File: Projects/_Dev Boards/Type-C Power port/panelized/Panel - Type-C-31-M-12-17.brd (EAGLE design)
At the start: 100 x 100 mm, 40 parts, among them J1 USB-TYPE-C-31-M-17, J10 USB-TYPE-C-31-M-12, J11 USB-TYPE-C-31-M-12, J12 USB-TYPE-C-31-M-12, J13 USB-TYPE-C-31-M-12, J14 USB-TYPE-C-31-M-12, J15 USB-TYPE-C-31-M-12, J16 USB-TYPE-C-31-M-17, J17 USB-TYPE-C-31-M-17, J18 USB-TYPE-C-31-M-17, J19 USB-TYPE-C-31-M-17, J2 USB-TYPE-C-31-M-12, J20 USB-TYPE-C-31-M-17, J3 USB-TYPE-C-31-M-17, J4 USB-TYPE-C-31-M-17, J5 USB-TYPE-C-31-M-17, J6 USB-TYPE-C-31-M-17, J7 USB-TYPE-C-31-M-12, J8 USB-TYPE-C-31-M-12, J9 USB-TYPE-C-31-M-12

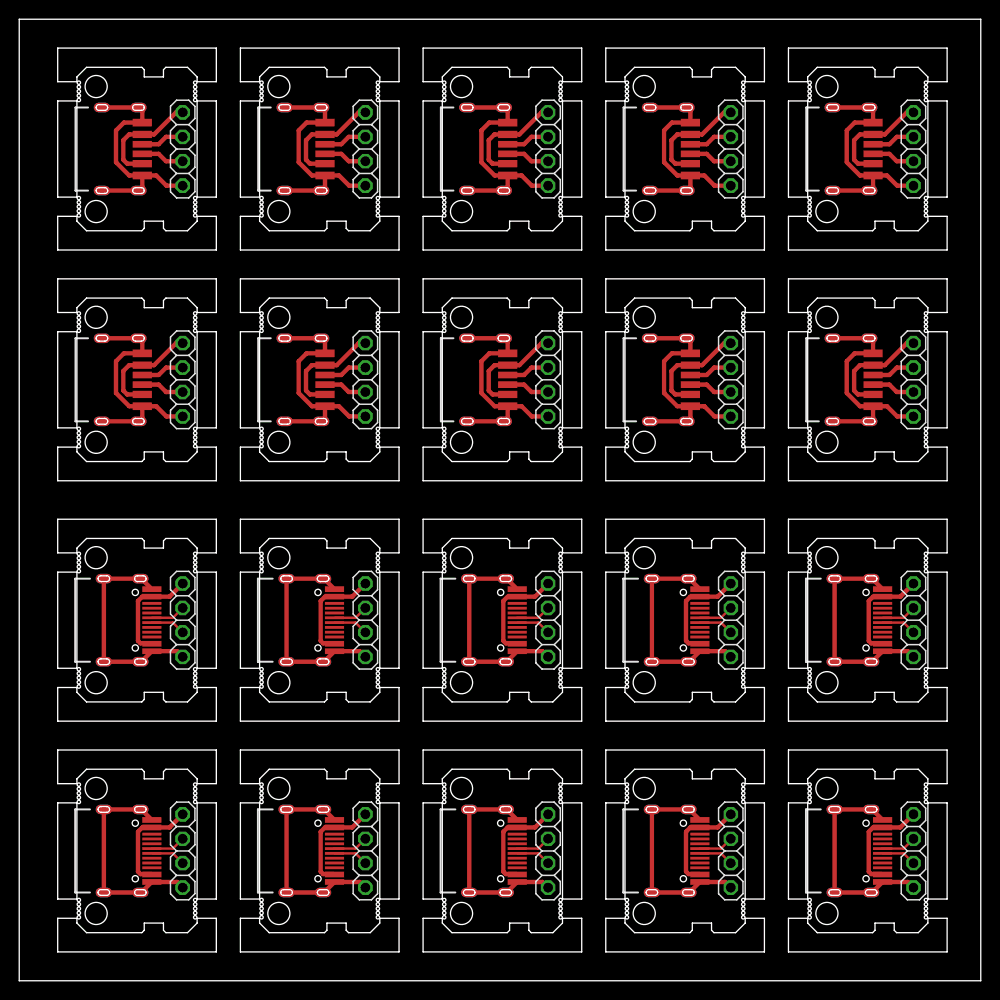
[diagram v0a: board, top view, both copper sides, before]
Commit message: updated Type-C power board
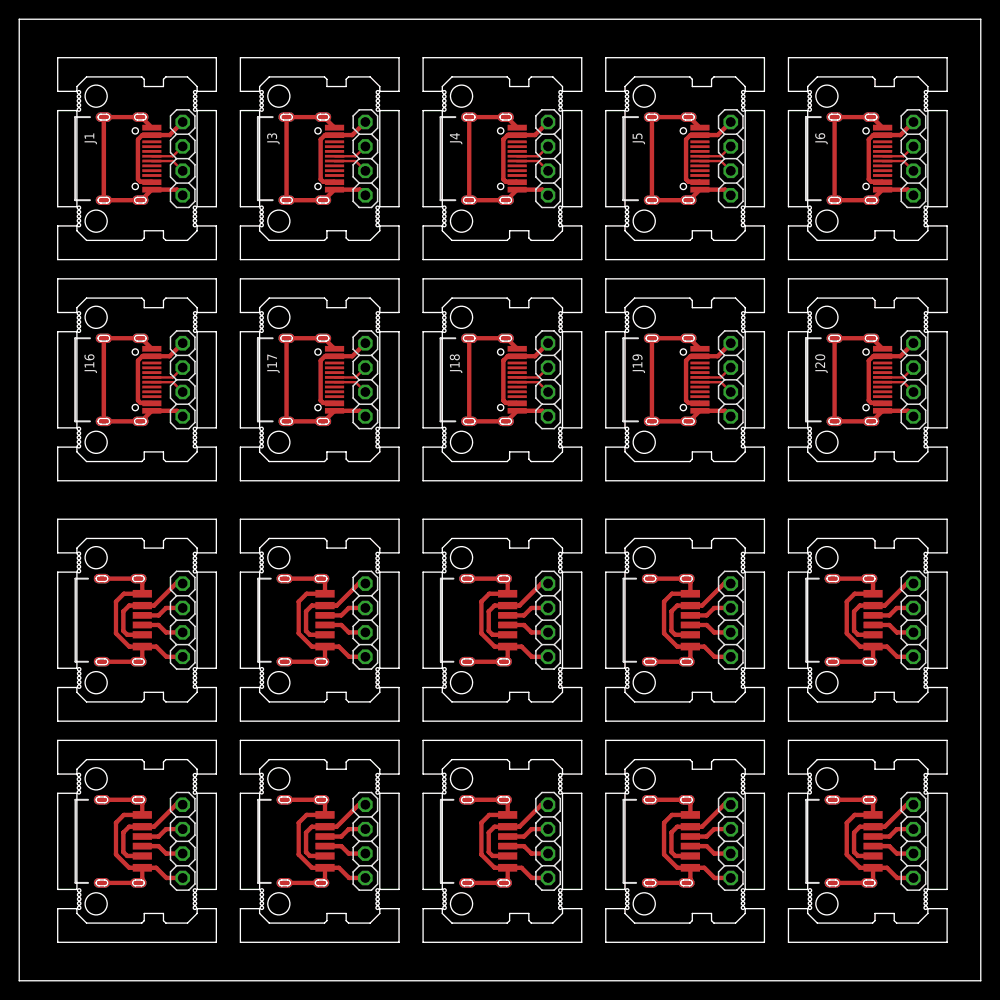
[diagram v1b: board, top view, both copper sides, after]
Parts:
- J1, J16, J17, J18, J19, J20, J3, J4, J5, J6: value USB-TYPE-C-31-M-17 -> USB-TYPE-C-31-M-12; device angrypig7-Connectors:USB-TYPE-C-31-M-17 -> angrypig7-Connectors:USB-TYPE-C-31-M-12
- J10, J11, J12, J13, J14, J15, J2, J7, J8, J9: value USB-TYPE-C-31-M-12 -> USB-TYPE-C-31-M-17; device angrypig7-Connectors:USB-TYPE-C-31-M-12 -> angrypig7-Connectors:USB-TYPE-C-31-M-17
- moved JP1 72.0 mm to (17.0, 14.5)
- moved JP2 72.0 mm to (17.0, 85.5)
- moved J3 1.02 mm to (31.6, 85.5)
- moved J4 1.02 mm to (50.6, 85.5)
- moved J7 1.02 mm to (31.4, 14.5)
- moved J8 1.02 mm to (50.4, 14.5)
- moved J1 1.02 mm to (12.6, 85.5)
- moved J2 1.02 mm to (12.4, 14.5)
- moved J10 1.02 mm to (88.4, 14.5)
- moved J5 1.02 mm to (69.6, 85.5)
- moved J6 1.02 mm to (88.6, 85.5)
- moved J9 1.02 mm to (69.4, 14.5)
- moved JP10 1.00 mm to (93.0, 14.5)
- moved JP3 1.00 mm to (36.0, 85.5)
- moved JP4 1.00 mm to (55.0, 85.5)
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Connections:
- new net N$61: J16.VBUS1, J16.VBUS2, JP16.1
- new net N$62: J16.A6, JP16.2
- new net N$63: J16.A7, JP16.3
- new net N$64: J16.GND1, J16.GND2, J16.SHLD-B1, J16.SHLD-B2, J16.SHLD-B3, J16.SHLD-B4, J16.SHLD-T1, J16.SHLD-T2, J16.SHLD-T3, J16.SHLD-T4, JP16.4
- new net N$65: J17.VBUS1, J17.VBUS2, JP17.1
- new net N$66: J17.A6, JP17.2
- new net N$67: J17.A7, JP17.3
- new net N$68: J17.GND1, J17.GND2, J17.SHLD-B1, J17.SHLD-B2, J17.SHLD-B3, J17.SHLD-B4, J17.SHLD-T1, J17.SHLD-T2, J17.SHLD-T3, J17.SHLD-T4, JP17.4
- new net N$69: J18.VBUS1, J18.VBUS2, JP18.1
- new net N$70: J18.A6, JP18.2
- new net N$71: J18.A7, JP18.3
- new net N$72: J18.GND1, J18.GND2, J18.SHLD-B1, J18.SHLD-B2, J18.SHLD-B3, J18.SHLD-B4, J18.SHLD-T1, J18.SHLD-T2, J18.SHLD-T3, J18.SHLD-T4, JP18.4
- new net N$73: J19.VBUS1, J19.VBUS2, JP19.1
- new net N$74: J19.A6, JP19.2
- new net N$75: J19.A7, JP19.3
- new net N$76: J19.GND1, J19.GND2, J19.SHLD-B1, J19.SHLD-B2, J19.SHLD-B3, J19.SHLD-B4, J19.SHLD-T1, J19.SHLD-T2, J19.SHLD-T3, J19.SHLD-T4, JP19.4
- new net N$77: J20.VBUS1, J20.VBUS2, JP20.1
- new net N$78: J20.A6, JP20.2
- new net N$79: J20.A7, JP20.3
- new net N$80: J20.GND1, J20.GND2, J20.SHLD-B1, J20.SHLD-B2, J20.SHLD-B3, J20.SHLD-B4, J20.SHLD-T1, J20.SHLD-T2, J20.SHLD-T3, J20.SHLD-T4, JP20.4
- net N$1: now also J1.VBUS1, J1.VBUS2, JP2.1; no longer J1.GND, J1.GND_2, J1.SHLD-B1, J1.SHLD-B2, J1.SHLD-B3, J1.SHLD-B4, J1.SHLD-T1, J1.SHLD-T2, J1.SHLD-T3, J1.SHLD-T4, JP1.4
- net N$10: now also J3.A6, JP3.2; no longer J3.VBUS, J3.VBUS_2, JP3.1
- net N$11: now also J3.A7, JP3.3; no longer J3.CC1, JP3.2
- net N$12: now also J3.GND1, J3.GND2, J3.SHLD-B1, J3.SHLD-B2, J3.SHLD-B3, J3.SHLD-B4, J3.SHLD-T1, J3.SHLD-T2, J3.SHLD-T3, J3.SHLD-T4, JP3.4; no longer J3.CC2, JP3.3
- net N$13: now also J4.VBUS1, J4.VBUS2, JP4.1; no longer J4.GND, J4.GND_2, J4.SHLD-B1, J4.SHLD-B2, J4.SHLD-B3, J4.SHLD-B4, J4.SHLD-T1, J4.SHLD-T2, J4.SHLD-T3, J4.SHLD-T4, JP4.4
- net N$14: now also J4.A6, JP4.2; no longer J4.VBUS, J4.VBUS_2, JP4.1
- net N$15: now also J4.A7, JP4.3; no longer J4.CC1, JP4.2
- net N$16: now also J4.GND1, J4.GND2, J4.SHLD-B1, J4.SHLD-B2, J4.SHLD-B3, J4.SHLD-B4, J4.SHLD-T1, J4.SHLD-T2, J4.SHLD-T3, J4.SHLD-T4, JP4.4; no longer J4.CC2, JP4.3
- net N$17: now also J5.VBUS1, J5.VBUS2, JP5.1; no longer J5.GND, J5.GND_2, J5.SHLD-B1, J5.SHLD-B2, J5.SHLD-B3, J5.SHLD-B4, J5.SHLD-T1, J5.SHLD-T2, J5.SHLD-T3, J5.SHLD-T4, JP5.4
- net N$18: now also J5.A6, JP5.2; no longer J5.VBUS, J5.VBUS_2, JP5.1
- net N$19: now also J5.A7, JP5.3; no longer J5.CC1, JP5.2
- net N$2: now also J1.A6, JP2.2; no longer J1.VBUS, J1.VBUS_2, JP1.1
- net N$20: now also J5.GND1, J5.GND2, J5.SHLD-B1, J5.SHLD-B2, J5.SHLD-B3, J5.SHLD-B4, J5.SHLD-T1, J5.SHLD-T2, J5.SHLD-T3, J5.SHLD-T4, JP5.4; no longer J5.CC2, JP5.3
- net N$21: now also J6.VBUS1, J6.VBUS2, JP6.1; no longer J6.GND, J6.GND_2, J6.SHLD-B1, J6.SHLD-B2, J6.SHLD-B3, J6.SHLD-B4, J6.SHLD-T1, J6.SHLD-T2, J6.SHLD-T3, J6.SHLD-T4, JP6.4
- net N$22: now also J6.A6, JP6.2; no longer J6.VBUS, J6.VBUS_2, JP6.1
- net N$23: now also J6.A7, JP6.3; no longer J6.CC1, JP6.2
- net N$24: now also J6.GND1, J6.GND2, J6.SHLD-B1, J6.SHLD-B2, J6.SHLD-B3, J6.SHLD-B4, J6.SHLD-T1, J6.SHLD-T2, J6.SHLD-T3, J6.SHLD-T4, JP6.4; no longer J6.CC2, JP6.3
- net N$25: now also J7.GND, J7.GND_2, J7.SHLD-B1, J7.SHLD-B2, J7.SHLD-B3, J7.SHLD-B4, J7.SHLD-T1, J7.SHLD-T2, J7.SHLD-T3, J7.SHLD-T4, JP7.4; no longer J7.VBUS1, J7.VBUS2, JP7.1
- net N$26: now also J7.VBUS, J7.VBUS_2, JP7.1; no longer J7.A6, JP7.2
- net N$27: now also J7.CC1, JP7.2; no longer J7.A7, JP7.3
- net N$28: now also J7.CC2, JP7.3; no longer J7.GND1, J7.GND2, J7.SHLD-B1, J7.SHLD-B2, J7.SHLD-B3, J7.SHLD-B4, J7.SHLD-T1, J7.SHLD-T2, J7.SHLD-T3, J7.SHLD-T4, JP7.4
- net N$29: now also J8.GND, J8.GND_2, J8.SHLD-B1, J8.SHLD-B2, J8.SHLD-B3, J8.SHLD-B4, J8.SHLD-T1, J8.SHLD-T2, J8.SHLD-T3, J8.SHLD-T4, JP8.4; no longer J8.VBUS1, J8.VBUS2, JP8.1
- net N$3: now also J1.A7, JP2.3; no longer J1.CC1, JP1.2
- net N$30: now also J8.VBUS, J8.VBUS_2, JP8.1; no longer J8.A6, JP8.2
- net N$31: now also J8.CC1, JP8.2; no longer J8.A7, JP8.3
- net N$32: now also J8.CC2, JP8.3; no longer J8.GND1, J8.GND2, J8.SHLD-B1, J8.SHLD-B2, J8.SHLD-B3, J8.SHLD-B4, J8.SHLD-T1, J8.SHLD-T2, J8.SHLD-T3, J8.SHLD-T4, JP8.4
- net N$33: now also J9.GND, J9.GND_2, J9.SHLD-B1, J9.SHLD-B2, J9.SHLD-B3, J9.SHLD-B4, J9.SHLD-T1, J9.SHLD-T2, J9.SHLD-T3, J9.SHLD-T4, JP9.4; no longer J9.VBUS1, J9.VBUS2, JP9.1
- net N$34: now also J9.VBUS, J9.VBUS_2, JP9.1; no longer J9.A6, JP9.2
- net N$35: now also J9.CC1, JP9.2; no longer J9.A7, JP9.3
- net N$36: now also J9.CC2, JP9.3; no longer J9.GND1, J9.GND2, J9.SHLD-B1, J9.SHLD-B2, J9.SHLD-B3, J9.SHLD-B4, J9.SHLD-T1, J9.SHLD-T2, J9.SHLD-T3, J9.SHLD-T4, JP9.4
- net N$37: now also J10.GND, J10.GND_2, J10.SHLD-B1, J10.SHLD-B2, J10.SHLD-B3, J10.SHLD-B4, J10.SHLD-T1, J10.SHLD-T2, J10.SHLD-T3, J10.SHLD-T4, JP10.4; no longer J10.VBUS1, J10.VBUS2, JP10.1
- net N$38: now also J10.VBUS, J10.VBUS_2, JP10.1; no longer J10.A6, JP10.2
- net N$39: now also J10.CC1, JP10.2; no longer J10.A7, JP10.3
- net N$4: now also J1.GND1, J1.GND2, J1.SHLD-B1, J1.SHLD-B2, J1.SHLD-B3, J1.SHLD-B4, J1.SHLD-T1, J1.SHLD-T2, J1.SHLD-T3, J1.SHLD-T4, JP2.4; no longer J1.CC2, JP1.3
- net N$40: now also J10.CC2, JP10.3; no longer J10.GND1, J10.GND2, J10.SHLD-B1, J10.SHLD-B2, J10.SHLD-B3, J10.SHLD-B4, J10.SHLD-T1, J10.SHLD-T2, J10.SHLD-T3, J10.SHLD-T4, JP10.4
- net N$41: now also J11.GND, J11.GND_2, J11.SHLD-B1, J11.SHLD-B2, J11.SHLD-B3, J11.SHLD-B4, J11.SHLD-T1, J11.SHLD-T2, J11.SHLD-T3, J11.SHLD-T4, JP11.4; no longer J11.VBUS1, J11.VBUS2, JP11.1
- net N$42: now also J11.VBUS, J11.VBUS_2, JP11.1; no longer J11.A6, JP11.2
- net N$43: now also J11.CC1, JP11.2; no longer J11.A7, JP11.3
- net N$44: now also J11.CC2, JP11.3; no longer J11.GND1, J11.GND2, J11.SHLD-B1, J11.SHLD-B2, J11.SHLD-B3, J11.SHLD-B4, J11.SHLD-T1, J11.SHLD-T2, J11.SHLD-T3, J11.SHLD-T4, JP11.4
- net N$45: now also J12.GND, J12.GND_2, J12.SHLD-B1, J12.SHLD-B2, J12.SHLD-B3, J12.SHLD-B4, J12.SHLD-T1, J12.SHLD-T2, J12.SHLD-T3, J12.SHLD-T4, JP12.4; no longer J12.VBUS1, J12.VBUS2, JP12.1
- net N$46: now also J12.VBUS, J12.VBUS_2, JP12.1; no longer J12.A6, JP12.2
- net N$47: now also J12.CC1, JP12.2; no longer J12.A7, JP12.3
- net N$48: now also J12.CC2, JP12.3; no longer J12.GND1, J12.GND2, J12.SHLD-B1, J12.SHLD-B2, J12.SHLD-B3, J12.SHLD-B4, J12.SHLD-T1, J12.SHLD-T2, J12.SHLD-T3, J12.SHLD-T4, JP12.4
- net N$49: now also J13.GND, J13.GND_2, J13.SHLD-B1, J13.SHLD-B2, J13.SHLD-B3, J13.SHLD-B4, J13.SHLD-T1, J13.SHLD-T2, J13.SHLD-T3, J13.SHLD-T4, JP13.4; no longer J13.VBUS1, J13.VBUS2, JP13.1
- net N$5: now also J2.GND, J2.GND_2, J2.SHLD-B1, J2.SHLD-B2, J2.SHLD-B3, J2.SHLD-B4, J2.SHLD-T1, J2.SHLD-T2, J2.SHLD-T3, J2.SHLD-T4, JP1.4; no longer J2.VBUS1, J2.VBUS2, JP2.1
- net N$50: now also J13.VBUS, J13.VBUS_2, JP13.1; no longer J13.A6, JP13.2
- net N$51: now also J13.CC1, JP13.2; no longer J13.A7, JP13.3
- net N$52: now also J13.CC2, JP13.3; no longer J13.GND1, J13.GND2, J13.SHLD-B1, J13.SHLD-B2, J13.SHLD-B3, J13.SHLD-B4, J13.SHLD-T1, J13.SHLD-T2, J13.SHLD-T3, J13.SHLD-T4, JP13.4
- net N$53: now also J14.GND, J14.GND_2, J14.SHLD-B1, J14.SHLD-B2, J14.SHLD-B3, J14.SHLD-B4, J14.SHLD-T1, J14.SHLD-T2, J14.SHLD-T3, J14.SHLD-T4, JP14.4; no longer J14.VBUS1, J14.VBUS2, JP14.1
- net N$54: now also J14.VBUS, J14.VBUS_2, JP14.1; no longer J14.A6, JP14.2
- net N$55: now also J14.CC1, JP14.2; no longer J14.A7, JP14.3
- net N$56: now also J14.CC2, JP14.3; no longer J14.GND1, J14.GND2, J14.SHLD-B1, J14.SHLD-B2, J14.SHLD-B3, J14.SHLD-B4, J14.SHLD-T1, J14.SHLD-T2, J14.SHLD-T3, J14.SHLD-T4, JP14.4
- net N$57: now also J15.GND, J15.GND_2, J15.SHLD-B1, J15.SHLD-B2, J15.SHLD-B3, J15.SHLD-B4, J15.SHLD-T1, J15.SHLD-T2, J15.SHLD-T3, J15.SHLD-T4, JP15.4; no longer J15.VBUS1, J15.VBUS2, JP15.1
- net N$58: now also J15.VBUS, J15.VBUS_2, JP15.1; no longer J15.A6, JP15.2
- net N$59: now also J15.CC1, JP15.2; no longer J15.A7, JP15.3
- net N$6: now also J2.VBUS, J2.VBUS_2, JP1.1; no longer J2.A6, JP2.2
- net N$60: now also J15.CC2, JP15.3; no longer J15.GND1, J15.GND2, J15.SHLD-B1, J15.SHLD-B2, J15.SHLD-B3, J15.SHLD-B4, J15.SHLD-T1, J15.SHLD-T2, J15.SHLD-T3, J15.SHLD-T4, JP15.4
- net N$7: now also J2.CC1, JP1.2; no longer J2.A7, JP2.3
- net N$8: now also J2.CC2, JP1.3; no longer J2.GND1, J2.GND2, J2.SHLD-B1, J2.SHLD-B2, J2.SHLD-B3, J2.SHLD-B4, J2.SHLD-T1, J2.SHLD-T2, J2.SHLD-T3, J2.SHLD-T4, JP2.4
- net N$9: now also J3.VBUS1, J3.VBUS2, JP3.1; no longer J3.GND, J3.GND_2, J3.SHLD-B1, J3.SHLD-B2, J3.SHLD-B3, J3.SHLD-B4, J3.SHLD-T1, J3.SHLD-T2, J3.SHLD-T3, J3.SHLD-T4, JP3.4
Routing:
- net N$8: track 23.0 -> 4.52 mm
- net N$60: track 23.0 -> 4.52 mm
- net N$56: track 23.0 -> 4.52 mm
- net N$52: track 23.0 -> 4.52 mm
- net N$40: track 23.0 -> 4.52 mm
- net N$36: track 23.0 -> 4.52 mm
- net N$32: track 23.0 -> 4.52 mm
- net N$28: track 23.0 -> 4.52 mm
- net N$48: track 23.0 -> 4.52 mm
- net N$24: track 4.52 -> 23.0 mm
- net N$20: track 4.52 -> 23.0 mm
- net N$80: track 4.52 -> 23.0 mm
- net N$76: track 4.52 -> 23.0 mm
- net N$72: track 4.52 -> 23.0 mm
- net N$44: track 23.0 -> 4.52 mm
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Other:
- outline, holes or cut-outs redrawn
- board text added: "CC1"
- board text added: "CC2"

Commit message: update
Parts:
- removed J10, J11, J12, J13, J14, J15, J7, J8, J9: USB-TYPE-C-31-M-17, angrypig7-Connectors:USB-TYPE-C-31-M-17
- removed J16, J17, J18, J19, J20, J4, J5, J6: USB-TYPE-C-31-M-12, angrypig7-Connectors:USB-TYPE-C-31-M-12
- removed JP10, JP11, JP12, JP13, JP14, JP15, JP16, JP17, JP18, JP19, JP20, JP4, JP5, JP6, JP7, JP8, JP9: (no value), pinhead_v2:1X04/OCT
- added R1, R2, R3, R4, R5, R6: 5.1k, angrypig7-RCL:R0603
- J1, J3: value USB-TYPE-C-31-M-12 -> USB-TYPE-C-31-M-17; device angrypig7-Connectors:USB-TYPE-C-31-M-12 -> angrypig7-Connectors:USB-TYPE-C-31-M-17
- JP1, JP2, JP3: device pinhead_v2:1X04/OCT -> angrypig7-Connectors-PinHeads:1X04
- moved J2 77.3 mm to (38.5, 87.3)
- moved JP1 72.8 mm to (19.0, 87.3)
- moved JP3 31.0 mm to (67.0, 87.3)
- moved J3 31.0 mm to (62.5, 87.3)
- moved JP2 26.0 mm to (43.0, 87.3)
- moved J1 2.64 mm to (14.5, 87.3)
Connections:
- removed net N$10: J3.A6, JP3.2
- removed net N$11: J3.A7, JP3.3
- removed net N$12: J3.GND1, J3.GND2, J3.SHLD-B1, J3.SHLD-B2, J3.SHLD-B3, J3.SHLD-B4, J3.SHLD-T1, J3.SHLD-T2, J3.SHLD-T3, J3.SHLD-T4, JP3.4
- removed net N$13: J4.VBUS1, J4.VBUS2, JP4.1
- removed net N$14: J4.A6, JP4.2
- removed net N$15: J4.A7, JP4.3
- removed net N$16: J4.GND1, J4.GND2, J4.SHLD-B1, J4.SHLD-B2, J4.SHLD-B3, J4.SHLD-B4, J4.SHLD-T1, J4.SHLD-T2, J4.SHLD-T3, J4.SHLD-T4, JP4.4
- removed net N$17: J5.VBUS1, J5.VBUS2, JP5.1
- removed net N$18: J5.A6, JP5.2
- removed net N$19: J5.A7, JP5.3
- removed net N$20: J5.GND1, J5.GND2, J5.SHLD-B1, J5.SHLD-B2, J5.SHLD-B3, J5.SHLD-B4, J5.SHLD-T1, J5.SHLD-T2, J5.SHLD-T3, J5.SHLD-T4, JP5.4
- removed net N$21: J6.VBUS1, J6.VBUS2, JP6.1
- removed net N$22: J6.A6, JP6.2
- removed net N$23: J6.A7, JP6.3
- removed net N$24: J6.GND1, J6.GND2, J6.SHLD-B1, J6.SHLD-B2, J6.SHLD-B3, J6.SHLD-B4, J6.SHLD-T1, J6.SHLD-T2, J6.SHLD-T3, J6.SHLD-T4, JP6.4
- removed net N$25: J7.GND, J7.GND_2, J7.SHLD-B1, J7.SHLD-B2, J7.SHLD-B3, J7.SHLD-B4, J7.SHLD-T1, J7.SHLD-T2, J7.SHLD-T3, J7.SHLD-T4, JP7.4
- removed net N$26: J7.VBUS, J7.VBUS_2, JP7.1
- removed net N$27: J7.CC1, JP7.2
- removed net N$28: J7.CC2, JP7.3
- removed net N$29: J8.GND, J8.GND_2, J8.SHLD-B1, J8.SHLD-B2, J8.SHLD-B3, J8.SHLD-B4, J8.SHLD-T1, J8.SHLD-T2, J8.SHLD-T3, J8.SHLD-T4, JP8.4
- removed net N$30: J8.VBUS, J8.VBUS_2, JP8.1
- removed net N$31: J8.CC1, JP8.2
- removed net N$32: J8.CC2, JP8.3
- removed net N$33: J9.GND, J9.GND_2, J9.SHLD-B1, J9.SHLD-B2, J9.SHLD-B3, J9.SHLD-B4, J9.SHLD-T1, J9.SHLD-T2, J9.SHLD-T3, J9.SHLD-T4, JP9.4
- removed net N$34: J9.VBUS, J9.VBUS_2, JP9.1
- removed net N$35: J9.CC1, JP9.2
- removed net N$36: J9.CC2, JP9.3
- removed net N$37: J10.GND, J10.GND_2, J10.SHLD-B1, J10.SHLD-B2, J10.SHLD-B3, J10.SHLD-B4, J10.SHLD-T1, J10.SHLD-T2, J10.SHLD-T3, J10.SHLD-T4, JP10.4
- removed net N$38: J10.VBUS, J10.VBUS_2, JP10.1
- removed net N$39: J10.CC1, JP10.2
- removed net N$40: J10.CC2, JP10.3
- removed net N$41: J11.GND, J11.GND_2, J11.SHLD-B1, J11.SHLD-B2, J11.SHLD-B3, J11.SHLD-B4, J11.SHLD-T1, J11.SHLD-T2, J11.SHLD-T3, J11.SHLD-T4, JP11.4
- removed net N$42: J11.VBUS, J11.VBUS_2, JP11.1
- removed net N$43: J11.CC1, JP11.2
- removed net N$44: J11.CC2, JP11.3
- removed net N$45: J12.GND, J12.GND_2, J12.SHLD-B1, J12.SHLD-B2, J12.SHLD-B3, J12.SHLD-B4, J12.SHLD-T1, J12.SHLD-T2, J12.SHLD-T3, J12.SHLD-T4, JP12.4
- removed net N$46: J12.VBUS, J12.VBUS_2, JP12.1
- removed net N$47: J12.CC1, JP12.2
- removed net N$48: J12.CC2, JP12.3
- removed net N$49: J13.GND, J13.GND_2, J13.SHLD-B1, J13.SHLD-B2, J13.SHLD-B3, J13.SHLD-B4, J13.SHLD-T1, J13.SHLD-T2, J13.SHLD-T3, J13.SHLD-T4, JP13.4
- removed net N$50: J13.VBUS, J13.VBUS_2, JP13.1
- removed net N$51: J13.CC1, JP13.2
- removed net N$52: J13.CC2, JP13.3
- removed net N$53: J14.GND, J14.GND_2, J14.SHLD-B1, J14.SHLD-B2, J14.SHLD-B3, J14.SHLD-B4, J14.SHLD-T1, J14.SHLD-T2, J14.SHLD-T3, J14.SHLD-T4, JP14.4
- removed net N$54: J14.VBUS, J14.VBUS_2, JP14.1
- removed net N$55: J14.CC1, JP14.2
- removed net N$56: J14.CC2, JP14.3
- removed net N$57: J15.GND, J15.GND_2, J15.SHLD-B1, J15.SHLD-B2, J15.SHLD-B3, J15.SHLD-B4, J15.SHLD-T1, J15.SHLD-T2, J15.SHLD-T3, J15.SHLD-T4, JP15.4
- removed net N$58: J15.VBUS, J15.VBUS_2, JP15.1
- removed net N$59: J15.CC1, JP15.2
- removed net N$60: J15.CC2, JP15.3
- removed net N$61: J16.VBUS1, J16.VBUS2, JP16.1
- removed net N$62: J16.A6, JP16.2
- removed net N$63: J16.A7, JP16.3
- removed net N$64: J16.GND1, J16.GND2, J16.SHLD-B1, J16.SHLD-B2, J16.SHLD-B3, J16.SHLD-B4, J16.SHLD-T1, J16.SHLD-T2, J16.SHLD-T3, J16.SHLD-T4, JP16.4
- removed net N$65: J17.VBUS1, J17.VBUS2, JP17.1
- removed net N$66: J17.A6, JP17.2
- removed net N$67: J17.A7, JP17.3
- removed net N$68: J17.GND1, J17.GND2, J17.SHLD-B1, J17.SHLD-B2, J17.SHLD-B3, J17.SHLD-B4, J17.SHLD-T1, J17.SHLD-T2, J17.SHLD-T3, J17.SHLD-T4, JP17.4
- removed net N$69: J18.VBUS1, J18.VBUS2, JP18.1
- removed net N$7: J2.CC1, JP1.2
- removed net N$70: J18.A6, JP18.2
- removed net N$71: J18.A7, JP18.3
- removed net N$72: J18.GND1, J18.GND2, J18.SHLD-B1, J18.SHLD-B2, J18.SHLD-B3, J18.SHLD-B4, J18.SHLD-T1, J18.SHLD-T2, J18.SHLD-T3, J18.SHLD-T4, JP18.4
- removed net N$73: J19.VBUS1, J19.VBUS2, JP19.1
- removed net N$74: J19.A6, JP19.2
- removed net N$75: J19.A7, JP19.3
- removed net N$76: J19.GND1, J19.GND2, J19.SHLD-B1, J19.SHLD-B2, J19.SHLD-B3, J19.SHLD-B4, J19.SHLD-T1, J19.SHLD-T2, J19.SHLD-T3, J19.SHLD-T4, JP19.4
- removed net N$77: J20.VBUS1, J20.VBUS2, JP20.1
- removed net N$78: J20.A6, JP20.2
- removed net N$79: J20.A7, JP20.3
- removed net N$8: J2.CC2, JP1.3
- removed net N$80: J20.GND1, J20.GND2, J20.SHLD-B1, J20.SHLD-B2, J20.SHLD-B3, J20.SHLD-B4, J20.SHLD-T1, J20.SHLD-T2, J20.SHLD-T3, J20.SHLD-T4, JP20.4
- removed net N$9: J3.VBUS1, J3.VBUS2, JP3.1
- new net GND: J1.GND, J1.GND_2, J1.SHLD-B1, J1.SHLD-B2, J1.SHLD-B3, J1.SHLD-B4, J1.SHLD-T1, J1.SHLD-T2, J1.SHLD-T3, J1.SHLD-T4, JP1.3, JP1.4, R1.2, R2.2
- new net GND1: J2.GND, J2.GND_2, J2.SHLD-B1, J2.SHLD-B2, J2.SHLD-B3, J2.SHLD-B4, J2.SHLD-T1, J2.SHLD-T2, J2.SHLD-T3, J2.SHLD-T4, JP2.3, JP2.4, R3.2, R4.2
- new net GND2: J3.GND, J3.GND_2, J3.SHLD-B1, J3.SHLD-B2, J3.SHLD-B3, J3.SHLD-B4, J3.SHLD-T1, J3.SHLD-T2, J3.SHLD-T3, J3.SHLD-T4, JP3.3, JP3.4, R5.2, R6.2
- new net VBUS: J1.VBUS, J1.VBUS_2, JP1.1, JP1.2
- new net VBUS1: J2.VBUS, J2.VBUS_2, JP2.1, JP2.2
- new net VBUS2: J3.VBUS, J3.VBUS_2, JP3.1, JP3.2
- net N$1: now also J1.CC1, R1.1; no longer J1.VBUS1, J1.VBUS2, JP2.1
- net N$2: now also J1.CC2, R2.1; no longer J1.A6, JP2.2
- net N$3: now also J2.CC1, R3.1; no longer J1.A7, JP2.3
- net N$4: now also J2.CC2, R4.1; no longer J1.GND1, J1.GND2, J1.SHLD-B1, J1.SHLD-B2, J1.SHLD-B3, J1.SHLD-B4, J1.SHLD-T1, J1.SHLD-T2, J1.SHLD-T3, J1.SHLD-T4, JP2.4
- net N$5: now also J3.CC1, R5.1; no longer J2.GND, J2.GND_2, J2.SHLD-B1, J2.SHLD-B2, J2.SHLD-B3, J2.SHLD-B4, J2.SHLD-T1, J2.SHLD-T2, J2.SHLD-T3, J2.SHLD-T4, JP1.4
- net N$6: now also J3.CC2, R6.1; no longer J2.VBUS, J2.VBUS_2, JP1.1
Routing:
- net N$57: track 25.4 -> 0.00 mm
- net N$53: track 25.4 -> 0.00 mm
- net N$37: track 25.4 -> 0.00 mm
- net N$33: track 25.4 -> 0.00 mm
- net N$41: track 25.4 -> 0.00 mm
- net N$45: track 25.4 -> 0.00 mm
- net N$25: track 25.4 -> 0.00 mm
- net N$49: track 25.4 -> 0.00 mm
- net N$29: track 25.4 -> 0.00 mm
- net N$80: track 23.0 -> 0.00 mm
- net N$76: track 23.0 -> 0.00 mm
- net N$72: track 23.0 -> 0.00 mm
- net N$24: track 23.0 -> 0.00 mm
- net N$20: track 23.0 -> 0.00 mm
- net N$16: track 23.0 -> 0.00 mm
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- added copper zone on layer 1, net GND
- added copper zone on layer 16, net GND
- added copper zone on layer 1, net GND1
- added copper zone on layer 16, net GND1
- added copper zone on layer 1, net GND2
- added copper zone on layer 16, net GND2
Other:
- outline, holes or cut-outs redrawn
- board text removed: "CC1"
- board text removed: "CC2"
- board text removed: "D+"
- board text removed: "D-"
